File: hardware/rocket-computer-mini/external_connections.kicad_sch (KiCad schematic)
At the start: 60 parts, among them J2 TBLH11-350-05-BK, J3 878321620, J4 B4B-PH-SM4-TB, Q3 DTC123J, Q4 DTC123J, Q5 DTC123J, Q6 DTC123J, Q9 PMPB14XNX, U10 TPN4R712MD, U26 TPS22811LRPWR, U28 TPS22811LRPWR, U6 TPN4R712MD, U7 TPN4R712MD, U8 TPN4R712MD, U9 CSD16323Q3

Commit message: hardware: C12 becomes a horizontal 2200uF can with a strap
Brings in the capacitor change authored in the objective-williams-12eae2
worktree, which had no commits of its own -- the work existed only as
uncommitted edits there.

The pyro energy store changes from the Nichicon EKYC160ELL103MM25S to a
Rubycon 2200uF 16V (16ZLH2200MEFC12.5X20) in a horizontal lay-down can with a
hold-down strap. That is a direct answer to the inherited fab notes' warning
about a can floating 4 mm above the board looking like a defect and the
instinct to seat it flush destroying the parts underneath -- lying down with a
strap removes the standoff entirely.

Carries the new footprint with it:
Footprints.pretty/CP_Radial_D12.5mm_L20.0mm_P5.00mm_Horizontal_Strap.kicad_mod
(4 pads -- two electrical, two plated mechanical for the strap). Per the
hardware README a new part must land in the same commit as the board that uses
it, or a clean clone breaks.

Incomplete as authored, and left that way: the schematic and BOM carry the new
part, but the PCB still has the old EKYC160ELL103MM25S footprint on C12.
Swapping it means re-placing and re-routing C12, which belongs with the layout
pass that is already owed for the P4 removal. Recorded in the board README.

ERC unchanged at 823.

Co-Authored-By: Claude Opus 5 <noreply@anthropic.com>
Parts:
- C12: value EKYC160ELL103MM25S -> 2200uF 16V; footprint Footprints:EKYC160ELL103MM25S -> Footprints:CP_Radial_D12.5mm_L20.0mm_P5.00mm_Horizontal_Strap; MPN EKYC160ELL103MM25S -> 16ZLH2200MEFC12.5X20; Mfr Nichicon -> Rubycon
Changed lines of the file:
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@@
 			)
 		)
-		(property "Value" "EKYC160ELL103MM25S"
+		(property "Value" "2200uF 16V"
 			(at 128.905 44.6531 0)
 			(show_name no)
@@
 			)
 		)
-		(property "Footprint" "Footprints:EKYC160ELL103MM25S"
+		(property "Footprint" "Footprints:CP_Radial_D12.5mm_L20.0mm_P5.00mm_Horizontal_Strap"
 			(at 125.73 43.815 0)
 			(hide yes)
@@
 			)
 		)
-		(property "MPN" "EKYC160ELL103MM25S"
+		(property "MPN" "16ZLH2200MEFC12.5X20"
 			(at 125.73 43.815 0)
 			(hide yes)
@@
 			)
 		)
-		(property "Mfr" "Nichicon"
+		(property "Mfr" "Rubycon"
 			(at 125.73 43.815 0)
 			(hide yes)

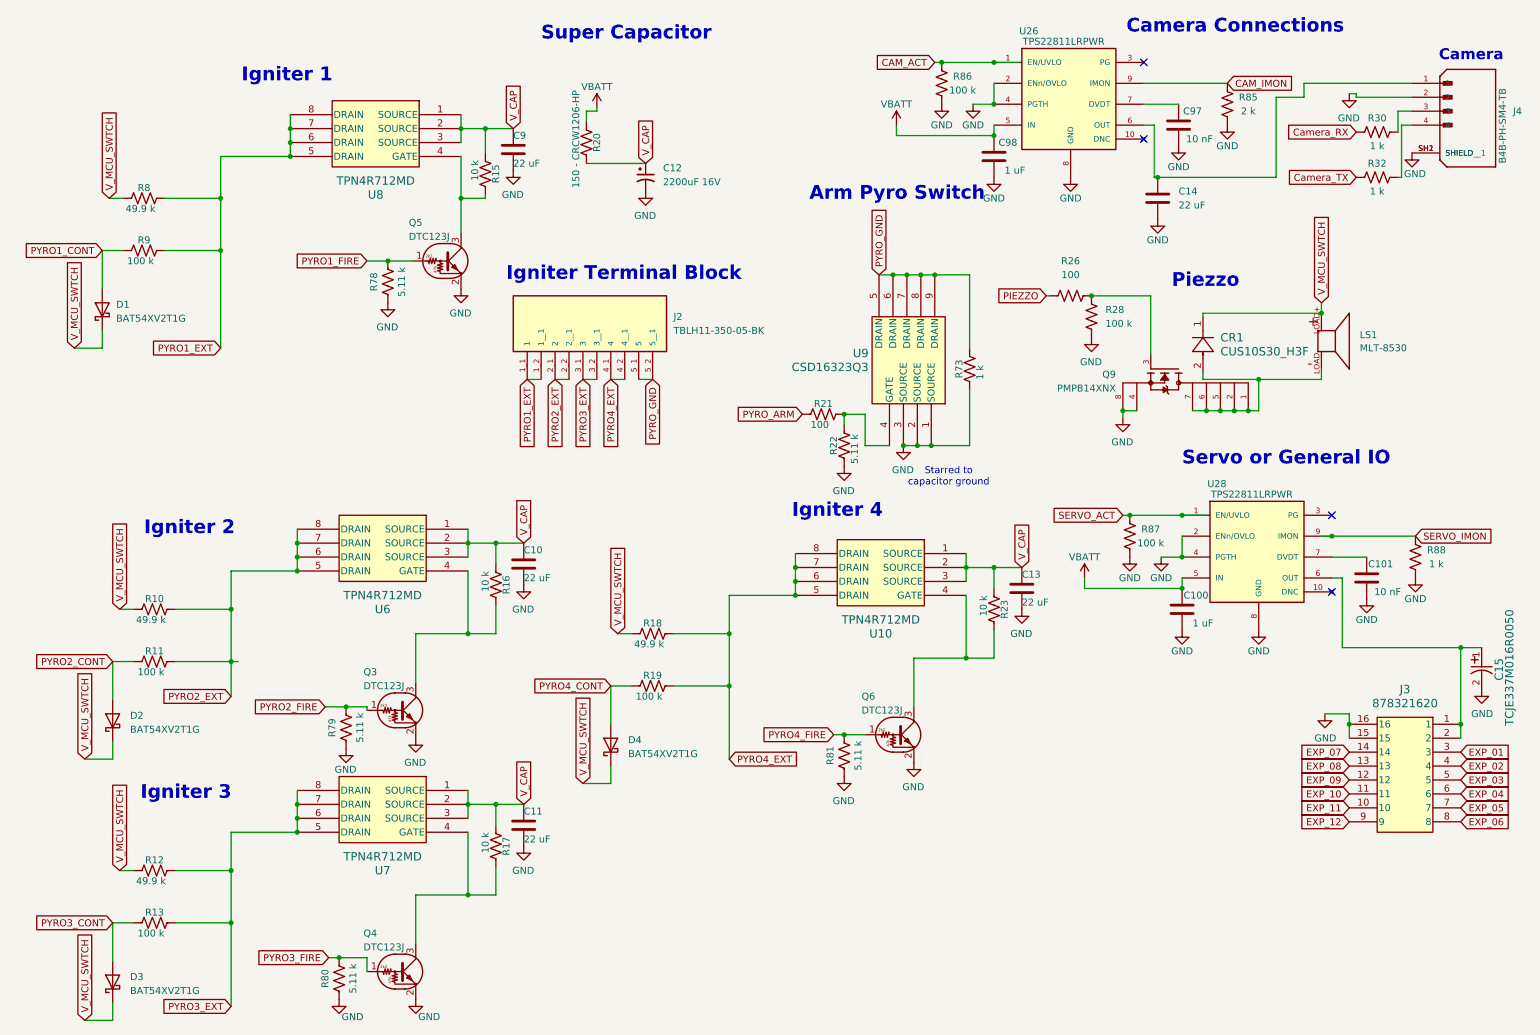
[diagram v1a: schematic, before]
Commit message: hardware: rocket-computer-mini gains the on-board radio, sheds more parts
Second reduction pass, plus the radio moves on-board.

Added: the 900 MHz radio module (U16) and its two decoupling caps, wired for
direct SPI rather than through the daughterboard connector. Removed: 31
designators including the camera connector (J4), the piezo (LS1), mounting
hardware (H5-H8), and the support parts that went with them. Also gone are the
magnetometer interrupt and the inertial sensor's second interrupt -- neither was
ever used by firmware, which is what made them free to drop.

Parts 190 -> 161, nets 191 -> 165.

Adds a pin budget for the reduced board (pin-budget.md). The headline is that
the board fits, but not comfortably: 23 signals against 27 usable pads, and only
16 of those pads are free of strapping, console, JTAG or flash-adjacent duty.

Three findings shaped it:

- The radio needs seven pins, not nine. DIO2 drives transmit-enable inside the
  module and needs no processor pin; receive-enable is floating and has no
  firmware pin at all. The out-computer firmware still carries the direct-SPI
  driver from the V7 topology and defines exactly those seven, so putting the
  bare module back on-board is a board change rather than a firmware rewrite.
- Pyro continuity is a digital read, not analogue, and nothing on this board
  needs an ADC channel -- so the ADC2-versus-radio restriction does not
  constrain the design.
- Continuity belongs on an I2C expander, not a multiplexer. A four-to-one mux
  needs two select lines plus data, saving one pin; the expander shares the bus
  the magnetometer is joining and saves four.

The proposed assignment keeps the serial console free and spends JTAG. Pyro
firing is confined to unrestricted pins -- never a strapping pin and never one
the boot ROM drives, since the console transmit pin is active on every boot.

One assumption can invalidate it: three signals sit on flash-adjacent pads that
are free only if the package carries no in-pa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
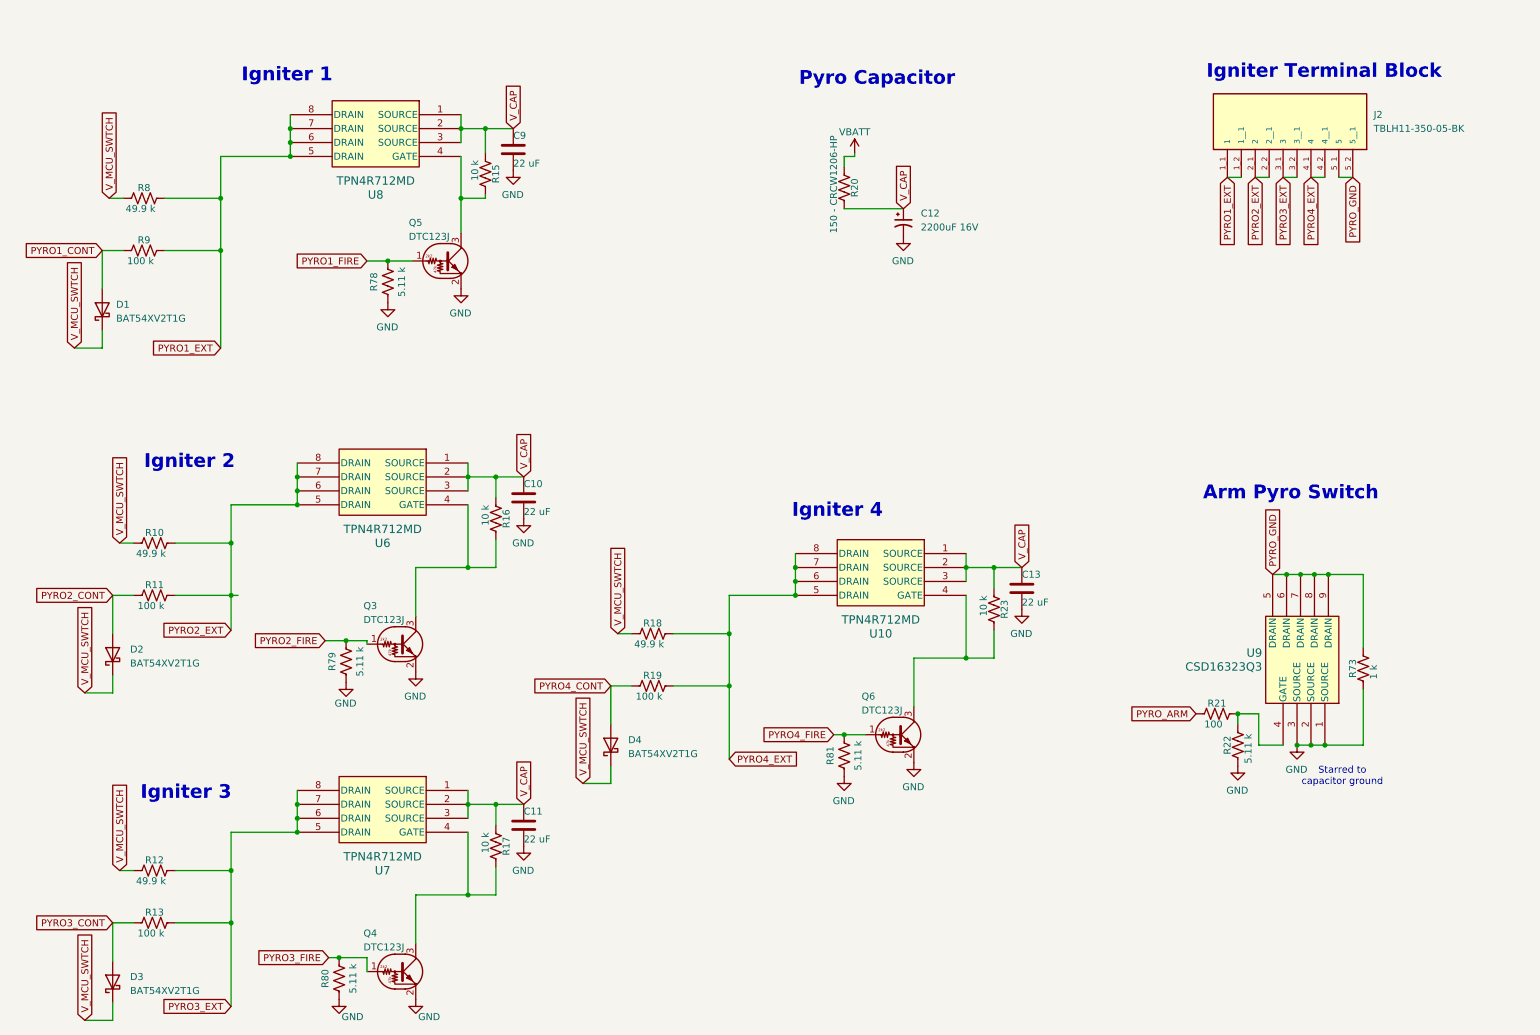
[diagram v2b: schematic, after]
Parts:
- removed C100, C98: 1 uF, Capacitor_SMD:C_0402_1005Metric, symbol Device:C
- removed C101, C97: 10 nF, Capacitor_SMD:C_0402_1005Metric, symbol Device:C
- removed C14: 22 uF, Capacitor_SMD:C_0805_2012Metric, symbol Device:C
- removed C15: TCJE337M016R0050, Footprints:CAPMP7.6X4.3_3.1N_KEM, symbol Custom:T491D227K016AT
- removed CR1: CUS10S30_H3F, Footprints:USC_TOS, symbol Custom:CUS10S30_H3F
- removed J3: 878321620, Footprints:CONN16_878321620_MOL, symbol Custom:878321620
- removed J4: B4B-PH-SM4-TB, Footprints:JST_B4B-PH-SM4-TB, symbol Custom:B4B-PH-SM4-TB
- removed LS1: MLT-8530, Footprints:BUZ_MLT-8530, symbol Custom:SMT-0540-T-9-R
- removed Q9: PMPB14XNX, Footprints:TRANS_PMPB14XNX, symbol Custom:PMPB14XNX
- removed R26: 100, Resistor_SMD:R_0402_1005Metric, symbol Device:R_US
- removed R28, R86, R87: 100 k, Resistor_SMD:R_0402_1005Metric, symbol Device:R_US
- removed R30, R32, R88: 1 k, Resistor_SMD:R_0402_1005Metric, symbol Device:R_US
- removed R85: 2 k, Resistor_SMD:R_0402_1005Metric, symbol Device:R_US
- removed U26, U28: TPS22811LRPWR, Footprints:IC_TPS22811LRPWR, symbol Custom:TPS22811LRPWR
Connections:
- no-connect marks 4 -> 0
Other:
- note added: "Pyro Capacitor"
- note removed: "Camera"
- note removed: "Camera Connections"
- note removed: "Piezzo"
- note removed: "Servo or General IO"
- note removed: "Super Capacitor"
- moved on the sheet: C10, C12, D2, J2, Q3, R10, R11, R16, R20, R21, R22, R73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
